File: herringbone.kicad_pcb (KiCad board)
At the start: 2 copper layers, 114.3 x 122.8 mm, 91 parts, among them U1 ATmega328P-PU, Y1 16MHz

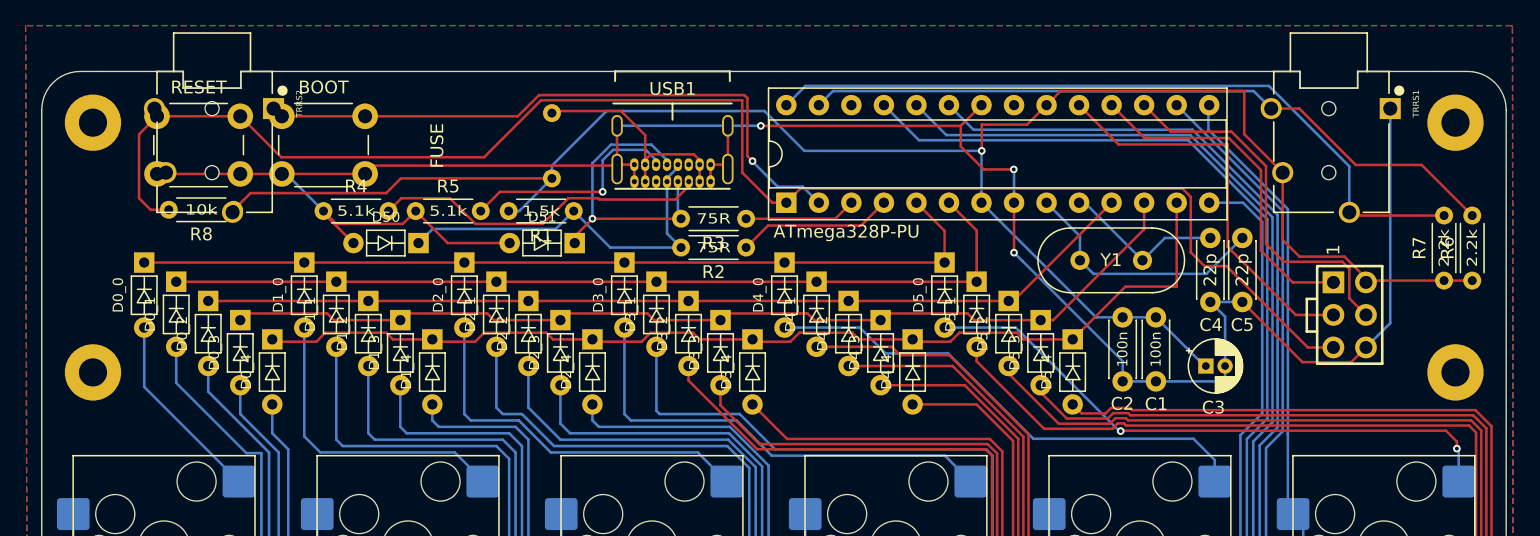
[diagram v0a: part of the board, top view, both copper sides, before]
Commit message: Second TRRS jack
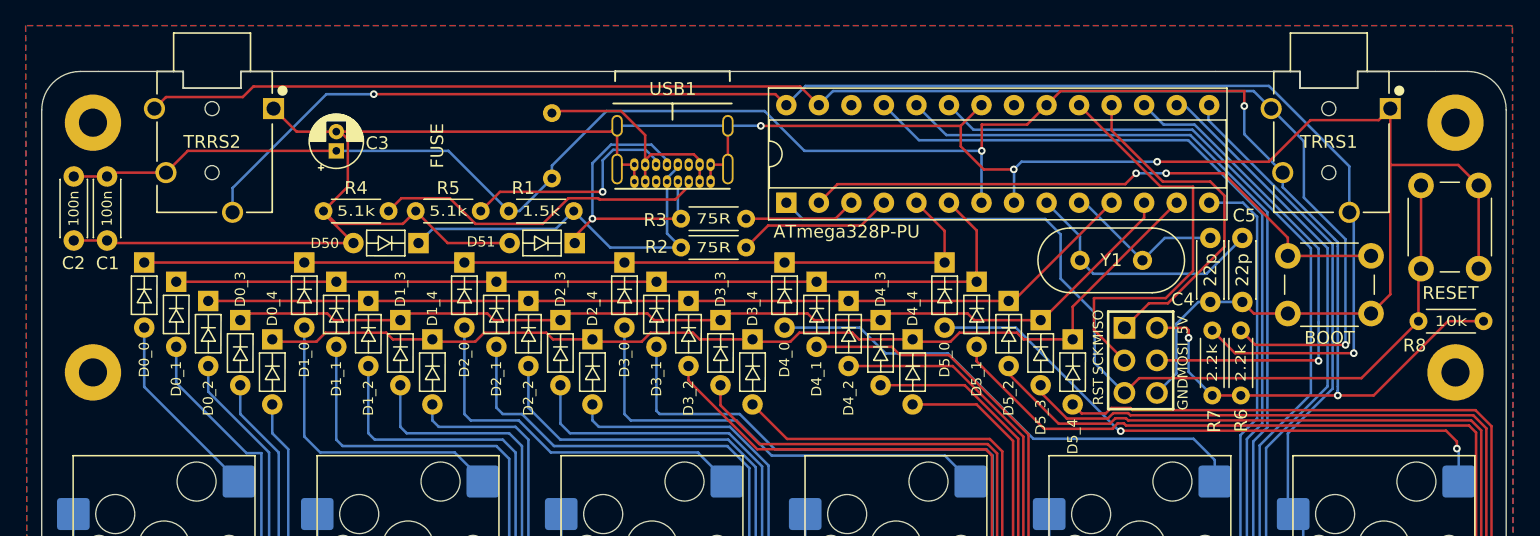
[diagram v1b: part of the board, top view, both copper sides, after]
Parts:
- moved B1 99.4 mm to (174.3, 54.5), turned to 90 degrees
- moved R8 98.0 mm to (179.2, 58.6)
- moved C1 82.6 mm to (71.8, 47.3)
- moved C2 82.6 mm to (69.2, 47.3)
- moved B2 79.3 mm to (163.9, 53.5)
- moved C3 69.9 mm to (89.7, 45.3), turned to 90 degrees
- moved R7 20.2 mm to (158.1, 64.4)
- moved R6 20.2 mm to (160.3, 64.4)
- moved ISP1 16.7 mm to (152.5, 61.7)
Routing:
- net i2c_SCL: track 57.9 -> 122.3 mm, vias 0 -> 2
- net i2c_SDA: track 55.5 -> 119.0 mm, vias 0 -> 1
- net RESET: track 119.5 -> 72.8 mm
- net GND: track 175.8 -> 211.4 mm
- net +5V: track 147.1 -> 165.3 mm, vias 1 -> 4
- net MOSI: track 29.0 -> 39.7 mm, vias 0 -> 1
- net COL0: track 300.8 -> 304.0 mm
- net COL5: track 110.7 -> 113.6 mm
- net ROW4: track 80.5 -> 78.2 mm
- net COL1: track 298.1 -> 300.2 mm
- net SCK: track 31.3 -> 32.6 mm
- net Net-(U1-PD0): track 48.8 -> 47.8 mm, vias 1 -> 2
- net MISO: track 26.7 -> 27.3 mm
- net ROW3: track 74.1 -> 73.6 mm
